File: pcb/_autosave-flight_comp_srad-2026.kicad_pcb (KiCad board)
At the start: 4 copper layers, 70 x 40 mm, 76 parts, among them J1 503398-1892, J2 Connector_3, J3 USB_B_Micro, J5 Vin_Bat, U1 IIM-20670, U3 RP2040, U4 ADXL375BCCZ-RL7, U5 MAX-M10M-00B, U6 W25Q128JVS, U7 XBP9B-DMSTB002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

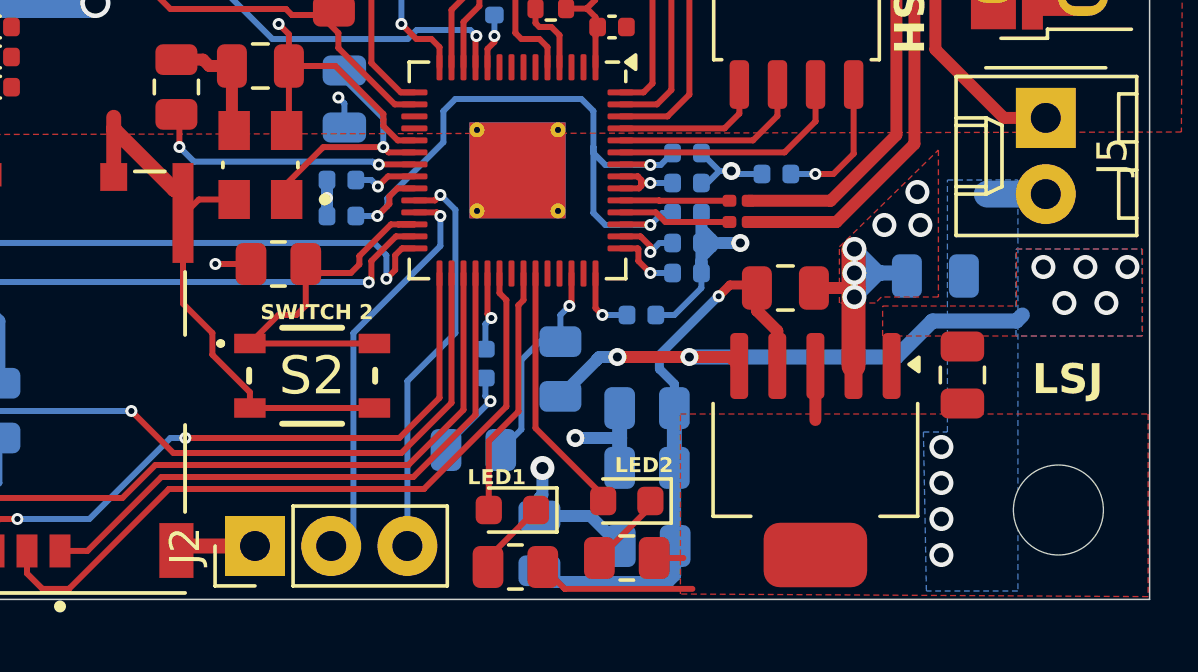
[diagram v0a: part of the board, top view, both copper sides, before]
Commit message: agregue beeper que falta conectar, saque vias abajo de pads y saque la filling zone gnd del bottom del regulador
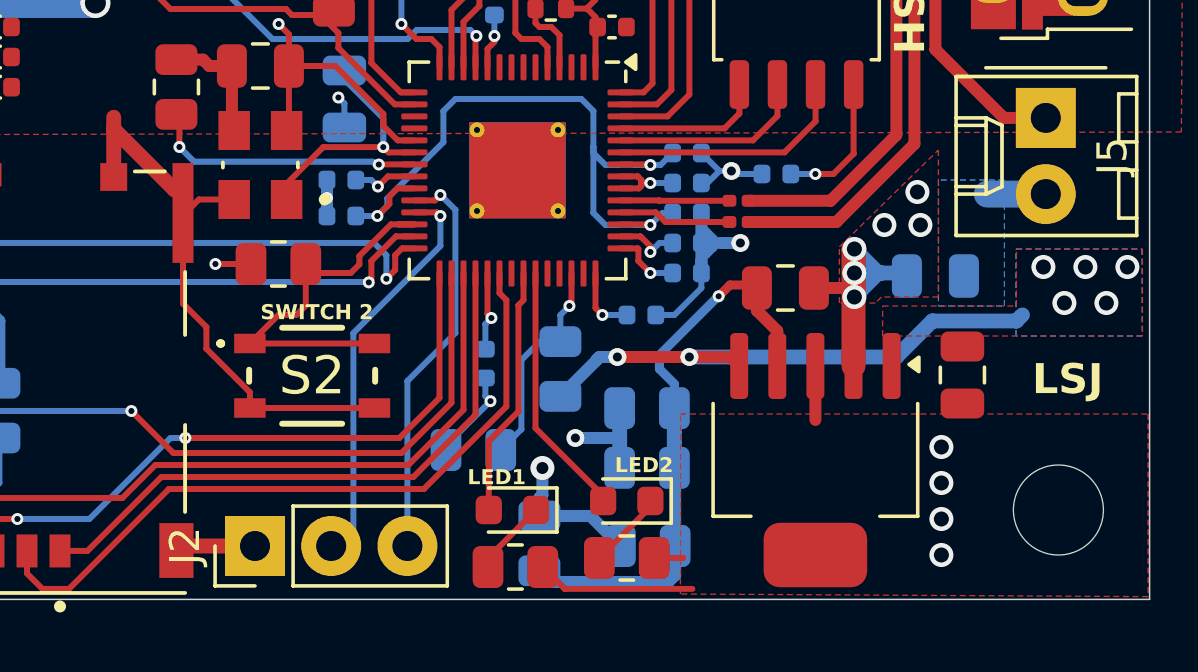
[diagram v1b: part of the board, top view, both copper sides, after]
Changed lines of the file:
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@@
 	)
 	(segment
+		(start 188.92 90.62)
+		(end 188.92 87.6)
+		(width 0.2)
+		(layer "F.Cu")
+		(net 4)
+	)
+	(segment
 		(start 191.15 94.1)
 		(end 195.3 94.1)
@@
 	)
 	(segment
-		(start 188.92 90.62)
-		(end 188.92 87.6)
-		(width 0.2)
-		(layer "F.Cu")
-		(net 4)
-	)
-	(segment
 		(start 186.2 61.65)
 		(end 186.325 61.525)
@@
 	)
 	(segment
+		(start 191.15 93.575)
+		(end 189.7 92.125)
+		(width 0.2)
+		(layer "F.Cu")
+		(net 4)
+	)
+	(segment
 		(start 191.32 98.7)
 		(end 188.85 98.7)
@@
 	)
 	(segment
-		(start 191.15 93.575)
-		(end 189.9 92.325)
+		(start 191.15 94.1)
+		(end 191.15 93.575)
 		(width 0.2)
 		(layer "F.Cu")
@@
 	)
 	(segment
+		(start 189.7 92.125)
+		(end 189.7 91.4)
+		(width 0.2)
+		(layer "F.Cu")
+		(net 4)
+	)
+	(segment
 		(start 185.72 61.65)
 		(end 186.2 61.65)
@@
 	)
 	(segment
+		(start 189.7 91.4)
+		(end 188.92 90.62)
+		(width 0.2)
+		(layer "F.Cu")
+		(net 4)
+	)
+	(segment
 		(start 217.3 75.2)
 		(end 217.4 75.3)
@@
 	)
 	(segment
-		(start 191.15 94.1)
-		(end 191.15 93.575)
-		(width 0.2)
-		(layer "F.Cu")
-		(net 4)
-	)
-	(segment
 		(start 181.26 68.01)
 		(end 181.26 69.1775)
@@
 	)
 	(segment
-		(start 189.9 92.325)
-		(end 189.9 91.6)
-		(width 0.2)
-		(layer "F.Cu")
-		(net 4)
-	)
-	(segment
-		(start 189.9 91.6)
-		(end 188.92 90.62)
-		(width 0.2)
-		(layer "F.Cu")
-		(net 4)
-	)
-	(segment
 		(start 185.63 61.36)
 		(end 185.62 61.37)
@@
 	)
 	(zone
-		(net 4)
-		(net_name "GND")
+		(net 2)
+		(net_name "VBUS")
 		(layer "B.Cu")
 		(hatch edge 0.5)
@@
 		(polygon
 			(pts
-				(xy 214.4 86.5) (xy 216.75 86.5) (xy 216.75 100.2) (xy 213.7 100.2) (xy 213.6 94.9) (xy 214.4 94.9)
+				(xy 216.686168 88.8) (xy 220.886168 88.8) (xy 220.9 91.7) (xy 216.686168 91.7)
 			)
 		)
 	)
 	(zone
-		(net 2)
-		(net_name "VBUS")
+		(net 4)
+		(net_name "GND")
 		(layer "B.Cu")
 		(hatch edge 0.5)
-		(priority 1)
-		(connect_pads yes
+		(priority 3)
+		(connect_pads
 			(clearance 0)
 		)
@@
 			(thermal_gap 0.5)
 			(thermal_bridge_width 0.5)
-			(island_removal_mode 1)
-			(island_area_min 10)
 		)
 		(polygon
 			(pts
-				(xy 216.686168 88.8) (xy 220.886168 88.8) (xy 220.9 91.7) (xy 216.686168 91.7)
+				(xy 216.3 86.5) (xy 214.1 86.5) (xy 214.1 90.7) (xy 216.3 90.7)
 			)
 		)
